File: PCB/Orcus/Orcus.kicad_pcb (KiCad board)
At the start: 2 copper layers, 258.2 x 87.7 mm, 84 parts, among them J1 -, J2 -, J3 +, J4 +, J5 LED, J6 LED, SW1 MX_LED, SW10 MX_LED, SW11 MX_LED, SW12 MX_LED, SW13 MX_LED, SW14 MX_LED, SW15 MX_LED, SW16 MX_LED, SW17 MX_LED, SW18 MX_LED, SW19 MX_LED, SW2 MX_LED, SW20 MX_LED, SW21 MX_LED, SW22 MX_LED, SW23 MX_LED, SW24 MX_LED, SW25 MX_LED, SW26 MX_LED, SW27 MX_LED, SW28 MX_LED, SW29 MX_LED, SW3 MX_LED, SW30 MX_LED, SW31 MX_LED, SW32 MX_LED, SW33 MX_LED, SW34 MX_LED, SW35 MX_LED, SW36 MX_LED, SW37 MX_LED, SW38 MX_LED, SW4 MX_LED, SW5 MX_LED, SW6 MX_LED, SW7 MX_LED, SW8 MX_LED, SW9 MX_LED, U1 XIAO-nRF52840-SMD, U3 XIAO-nRF52840-SMD

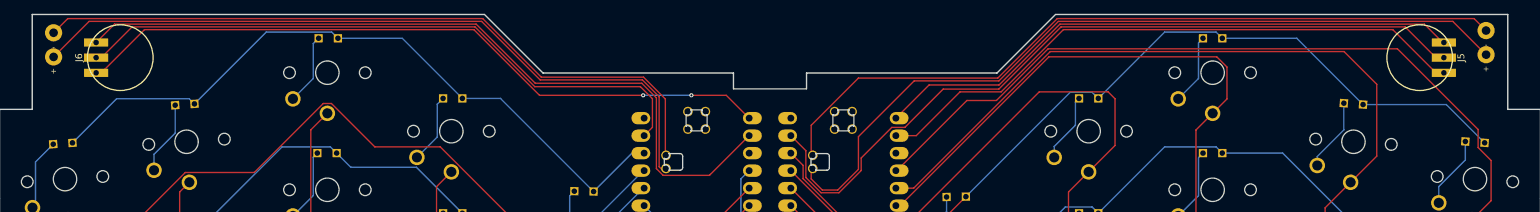
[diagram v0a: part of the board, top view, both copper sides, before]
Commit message: replaced pad
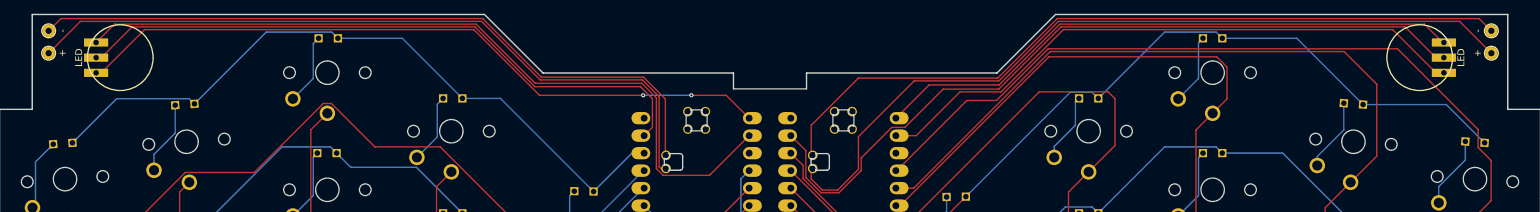
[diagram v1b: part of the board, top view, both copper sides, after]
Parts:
- +: renamed from J3; footprint TOTEMlib:BatteryPad -> Keebio-Parts.pretty-master:Wire_Pad_24AWG
- +: renamed from J4; footprint TOTEMlib:BatteryPad -> Keebio-Parts.pretty-master:Wire_Pad_24AWG
- -: renamed from J2; footprint TOTEMlib:BatteryPad -> Keebio-Parts.pretty-master:Wire_Pad_24AWG
- -: renamed from J1; footprint TOTEMlib:BatteryPad -> Keebio-Parts.pretty-master:Wire_Pad_24AWG
- moved + 0.90 mm to (42.9, 37.9), turned to -90 degrees
- moved + 0.80 mm to (252.4, 37.9), turned to 90 degrees
- moved - 0.78 mm to (42.9, 34.6), turned to -90 degrees
- moved - 0.77 mm to (252.4, 34.6), turned to 90 degrees
- renumbered J5 to LED, J6 to LED
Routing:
- net Net-(J1-Pin_1): track 109.3 -> 110.0 mm
- net Net-(J3-Pin_1): track 114.9 -> 115.6 mm
- net Net-(J2-Pin_1): track 102.1 -> 102.7 mm

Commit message: updated pcb and sch
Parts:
- removed LED (x2): LED, Keebio-Parts.pretty-master:NeoPixel_Mini_Button-v2
- added J5: LED, Keebio-Parts.pretty-master:NeoPixel_Mini_Button-v2, F.Cu at (242.0, 38.5)
- added J6: LED, Keebio-Parts.pretty-master:NeoPixel_Mini_Button-v2, F.Cu at (53.3, 38.5)
- D1, D10, D11, D12, D13, D14, D15, D16, D17, D18, D19, D2, D20, D21, D22, D23, D24, D25, D26, D27, D28, D29, D3, D30, D31, D32, D33, D34, D35, D36, D37, D38, D4, D5, D6, D7, D8, D9: footprint Keebio-Parts.pretty-master:D_SOD123F-Hole -> Keebio-Parts.pretty-master:D_SOD123F
- moved D30 6.89 mm to (133.3, 76.4), turned to -91 degrees
- moved D6 6.61 mm to (161.9, 76.2), turned to 91 degrees
- turned SW30 to 89 degrees
- turned SW6 to -89 degrees
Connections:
- U1 pad 1: unconnected-(U1-PA02_A0_D0-Pad1) -> row0-1
- U1 pad 10: col3-1 -> unconnected-(U1-PA5_A9_D9_MISO-Pad10)
- U1 pad 11: col4-1 -> Data-1
- U1 pad 2: Data-1 -> row1-1
- U1 pad 3: row0-1 -> row2-1
- U1 pad 4: row1-1 -> row3-1
- U1 pad 5: row2-1 -> col2-1
- U1 pad 6: row3-1 -> col1-1
- U1 pad 8: col1-1 -> col3-1
- U1 pad 9: col2-1 -> col4-1
- U3 pad 1: unconnected-(U3-PA02_A0_D0-Pad1) -> row0
- U3 pad 10: col3 -> unconnected-(U3-PA5_A9_D9_MISO-Pad10)
- U3 pad 11: col4 -> Data
- U3 pad 2: Data -> row1
- U3 pad 3: row0 -> row2
- U3 pad 4: row1 -> row3
- U3 pad 5: row2 -> col2
- U3 pad 6: row3 -> col1
- U3 pad 8: col1 -> col3
- U3 pad 9: col2 -> col4
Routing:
- net col1-1: track 194.9 -> 158.4 mm
- net col2-1: track 160.4 -> 130.6 mm, vias 0 -> 1
- net col0-1: track 152.4 -> 177.7 mm
- net col3: track 163.6 -> 144.1 mm
- net Data: track 113.4 -> 94.6 mm
- net Data-1: track 92.8 -> 110.6 mm
- net col4: track 166.0 -> 151.5 mm
- net col4-1: track 87.1 -> 96.8 mm
- net row2: track 134.5 -> 141.2 mm
- net col2: track 141.0 -> 147.3 mm
- net row0-1: track 102.2 -> 108.4 mm
- net row2-1: track 127.1 -> 132.7 mm
- net row3: track 144.5 -> 149.7 mm
- net row1-1: track 115.7 -> 120.7 mm
- net row1: track 126.2 -> 130.1 mm
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- added copper zone on B.Cu, net (none)
- added copper zone on F.Cu, net (none)

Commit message: update pcb
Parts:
- added Ref**: Mouse_Bite, Keebio-Parts.pretty-master:MouseBites_6x05mm_P1mm_Verical, F.Cu at (147.6, 67.5)
- moved U1 1.00 mm to (137.0, 53.9)
- moved U3 1.00 mm to (158.3, 53.9)
- renumbered J5 to LED, J6 to LED
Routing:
- net row1: track 130.1 -> 131.3 mm
- net Net-(J3-Pin_1): track 114.3 -> 115.4 mm
- net Net-(J4-Pin_1): track 105.3 -> 104.3 mm
- net row3: track 149.7 -> 150.7 mm
- net row2: track 141.2 -> 142.2 mm
- net row1-1: track 120.7 -> 121.7 mm
- net col4-1: track 96.8 -> 97.8 mm
- net col0: track 91.6 -> 92.6 mm
- net Net-(J2-Pin_1): track 102.3 -> 101.3 mm
- net row3-1: track 152.4 -> 153.4 mm
- net 5v-1: track 102.3 -> 103.2 mm
- net col0-1: track 177.7 -> 178.3 mm
- net row2-1: track 132.7 -> 133.3 mm
- net Data-1: track 110.6 -> 111.1 mm

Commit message: new sch
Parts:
- removed + (x2): +, Keebio-Parts.pretty-master:Wire_Pad_24AWG
- removed - (x2): -, Keebio-Parts.pretty-master:Wire_Pad_24AWG
- removed D1, D10, D11, D12, D13, D14, D15, D16, D17, D18, D19, D2, D20, D21, D22, D23, D24, D25, D26, D27, D28, D29, D3, D30, D31, D32, D33, D34, D35, D36, D37, D38, D4, D5, D6, D7, D8, D9: D, Keebio-Parts.pretty-master:D_SOD123F
- removed LED (x2): LED, Keebio-Parts.pretty-master:NeoPixel_Mini_Button-v2
- removed Ref**: Mouse_Bite, Keebio-Parts.pretty-master:MouseBites_6x05mm_P1mm_Verical
- removed SW1, SW10, SW11, SW12, SW13, SW14, SW15, SW16, SW17, SW18, SW19, SW2, SW20, SW21, SW22, SW23, SW24, SW25, SW26, SW27, SW28, SW29, SW3, SW30, SW31, SW32, SW33, SW34, SW35, SW36, SW37, SW38, SW4, SW5, SW6, SW7, SW8, SW9: MX_LED, Keebio-Parts.pretty-master:Kailh-PG1350-1u-NoLED
- removed U1, U3: XIAO-nRF52840-SMD, TOTEMlib:xiao-ble-smd-cutout-mod
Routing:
- net col0-1: track 178.3 -> 0.00 mm
- net col1-1: track 158.0 -> 0.00 mm
- net row3-1: track 153.4 -> 0.00 mm
- net col4: track 151.1 -> 0.00 mm
- net row3: track 150.7 -> 0.00 mm
- net col2: track 147.7 -> 0.00 mm
- net col3: track 143.7 -> 0.00 mm
- net row2: track 142.2 -> 0.00 mm
- net row2-1: track 133.3 -> 0.00 mm
- net row1: track 131.3 -> 0.00 mm
- net col2-1: track 130.1 -> 0.00 mm, vias 1 -> 0
- net row0: track 123.3 -> 0.00 mm
- net row1-1: track 121.7 -> 0.00 mm
- net Net-(J3-Pin_1): track 115.4 -> 0.00 mm
- net Gnd-1: track 112.6 -> 0.00 mm
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- removed copper zone on B.Cu, net (none)
- removed copper zone on F.Cu, net (none)
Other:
- board outline removed

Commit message: updated pcb
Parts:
- added D1: D, Keebio-Parts.pretty-master:D_SOD123F, B.Cu at (218.5, 105.0)
- added D10: D, Keebio-Parts.pretty-master:D_SOD123F, B.Cu at (211.5, 105.0)
- added D11: D, Keebio-Parts.pretty-master:D_SOD123F, B.Cu at (204.5, 94.5)
- added D12: D, Keebio-Parts.pretty-master:D_SOD123F, B.Cu at (204.5, 97.1)
- added D13: D, Keebio-Parts.pretty-master:D_SOD123F, B.Cu at (204.5, 99.7)
- added D14: D, Keebio-Parts.pretty-master:D_SOD123F, B.Cu at (204.5, 102.5)
- added D15: D, Keebio-Parts.pretty-master:D_SOD123F, B.Cu at (204.5, 105.1)
- added D16: D, Keebio-Parts.pretty-master:D_SOD123F, B.Cu at (197.5, 99.7)
- added D17: D, Keebio-Parts.pretty-master:D_SOD123F, B.Cu at (197.5, 94.5)
- added D18: D, Keebio-Parts.pretty-master:D_SOD123F, B.Cu at (197.5, 97.1)
- added D19: D, Keebio-Parts.pretty-master:D_SOD123F, B.Cu at (197.5, 102.5)
- added D2: D, Keebio-Parts.pretty-master:D_SOD123F, B.Cu at (218.5, 102.5)
- added D20: D, Keebio-Parts.pretty-master:D_SOD123F, F.Cu at (38.5, -7.50)
- added D21: D, Keebio-Parts.pretty-master:D_SOD123F, F.Cu at (37.3, -2.91)
- added D22: D, Keebio-Parts.pretty-master:D_SOD123F, F.Cu at (37.3, -0.31)
- added D23: D, Keebio-Parts.pretty-master:D_SOD123F, F.Cu at (37.3, 2.29)
- added D24: D, Keebio-Parts.pretty-master:D_SOD123F, F.Cu at (37.3, 4.89)
- added D25: D, Keebio-Parts.pretty-master:D_SOD123F, F.Cu at (37.3, 7.49)
- added D26: D, Keebio-Parts.pretty-master:D_SOD123F, F.Cu at (37.3, 10.1)
- added D27: D, Keebio-Parts.pretty-master:D_SOD123F, F.Cu at (37.3, 12.7)
- added D28: D, Keebio-Parts.pretty-master:D_SOD123F, F.Cu at (37.3, 15.3)
- added D29: D, Keebio-Parts.pretty-master:D_SOD123F, F.Cu at (37.3, 17.9)
- added D3: D, Keebio-Parts.pretty-master:D_SOD123F, B.Cu at (218.5, 99.7)
- added D30: D, Keebio-Parts.pretty-master:D_SOD123F, F.Cu at (37.3, 20.5)
- added D31: D, Keebio-Parts.pretty-master:D_SOD123F, F.Cu at (43.3, -2.91)
- added D32: D, Keebio-Parts.pretty-master:D_SOD123F, F.Cu at (43.3, -0.31)
- added D33: D, Keebio-Parts.pretty-master:D_SOD123F, F.Cu at (43.3, 2.29)
- added D34: D, Keebio-Parts.pretty-master:D_SOD123F, F.Cu at (43.3, 4.89)
- added D35: D, Keebio-Parts.pretty-master:D_SOD123F, F.Cu at (43.3, 7.49)
- added D36: D, Keebio-Parts.pretty-master:D_SOD123F, F.Cu at (43.3, 10.1)
- added D37: D, Keebio-Parts.pretty-master:D_SOD123F, F.Cu at (43.3, 12.7)
- added D38: D, Keebio-Parts.pretty-master:D_SOD123F, F.Cu at (43.3, 15.3)
- added D4: D, Keebio-Parts.pretty-master:D_SOD123F, B.Cu at (218.5, 97.0)
- added D5: D, Keebio-Parts.pretty-master:D_SOD123F, B.Cu at (218.5, 94.5)
- added D6: D, Keebio-Parts.pretty-master:D_SOD123F, B.Cu at (211.5, 94.5)
- added D7: D, Keebio-Parts.pretty-master:D_SOD123F, B.Cu at (211.5, 97.1)
- added D8: D, Keebio-Parts.pretty-master:D_SOD123F, B.Cu at (211.5, 99.7)
- added D9: D, Keebio-Parts.pretty-master:D_SOD123F, B.Cu at (211.5, 102.3)
- added SW1: MX_LED, Keebio-Parts.pretty-master:Kailh-PG1350-1u-NoLED, F.Cu at (178.7, 63.2)
- added SW10: MX_LED, Keebio-Parts.pretty-master:Kailh-PG1350-1u-NoLED, F.Cu at (252.8, 73.1)
- added SW11: MX_LED, Keebio-Parts.pretty-master:Kailh-PG1350-1u-NoLED, F.Cu at (179.3, 97.2)
- added SW12: MX_LED, Keebio-Parts.pretty-master:Kailh-PG1350-1u-NoLED, F.Cu at (197.9, 83.2)
- added SW13: MX_LED, Keebio-Parts.pretty-master:Kailh-PG1350-1u-NoLED, F.Cu at (215.9, 74.7)
- added SW14: MX_LED, Keebio-Parts.pretty-master:Kailh-PG1350-1u-NoLED, F.Cu at (233.9, 84.7)
- added SW15: MX_LED, Keebio-Parts.pretty-master:Kailh-PG1350-1u-NoLED, F.Cu at (251.5, 90.1)
- added SW16: MX_LED, Keebio-Parts.pretty-master:Kailh-PG1350-1u-NoLED, F.Cu at (161.3, 76.2)
- added SW17: MX_LED, Keebio-Parts.pretty-master:Kailh-PG1350-1u-NoLED, F.Cu at (232.3, 105.9)
- added SW18: MX_LED, Keebio-Parts.pretty-master:Kailh-PG1350-1u-NoLED, F.Cu at (250.2, 107.0)
- added SW19: MX_LED, Keebio-Parts.pretty-master:Kailh-PG1350-1u-NoLED, F.Cu at (269.7, 104.7)
- added SW2: MX_LED, Keebio-Parts.pretty-master:Kailh-PG1350-1u-NoLED, F.Cu at (197.9, 49.2)
- added SW20: MX_LED, Keebio-Parts.pretty-master:Kailh-PG1350-1u-NoLED, F.Cu at (117.6, 63.2)
- added SW21: MX_LED, Keebio-Parts.pretty-master:Kailh-PG1350-1u-NoLED, F.Cu at (98.4, 49.2)
- added SW22: MX_LED, Keebio-Parts.pretty-master:Kailh-PG1350-1u-NoLED, F.Cu at (80.4, 40.7)
- added SW23: MX_LED, Keebio-Parts.pretty-master:Kailh-PG1350-1u-NoLED, F.Cu at (60.0, 50.7)
- added SW24: MX_LED, Keebio-Parts.pretty-master:Kailh-PG1350-1u-NoLED, F.Cu at (42.3, 56.2)
- added SW25: MX_LED, Keebio-Parts.pretty-master:Kailh-PG1350-1u-NoLED, F.Cu at (117.3, 80.2)
- added SW26: MX_LED, Keebio-Parts.pretty-master:Kailh-PG1350-1u-NoLED, F.Cu at (98.4, 66.2)
- added SW27: MX_LED, Keebio-Parts.pretty-master:Kailh-PG1350-1u-NoLED, F.Cu at (80.4, 57.7)
- added SW28: MX_LED, Keebio-Parts.pretty-master:Kailh-PG1350-1u-NoLED, F.Cu at (61.2, 67.7)
- added SW29: MX_LED, Keebio-Parts.pretty-master:Kailh-PG1350-1u-NoLED, F.Cu at (43.6, 73.1)
- added SW3: MX_LED, Keebio-Parts.pretty-master:Kailh-PG1350-1u-NoLED, F.Cu at (215.9, 40.7)
- added SW30: MX_LED, Keebio-Parts.pretty-master:Kailh-PG1350-1u-NoLED, F.Cu at (117.0, 97.2)
- added SW31: MX_LED, Keebio-Parts.pretty-master:Kailh-PG1350-1u-NoLED, F.Cu at (98.4, 83.2)
- added SW32: MX_LED, Keebio-Parts.pretty-master:Kailh-PG1350-1u-NoLED, F.Cu at (80.4, 74.7)
- added SW33: MX_LED, Keebio-Parts.pretty-master:Kailh-PG1350-1u-NoLED, F.Cu at (62.5, 84.7)
- added SW34: MX_LED, Keebio-Parts.pretty-master:Kailh-PG1350-1u-NoLED, F.Cu at (44.8, 90.1)
- added SW35: MX_LED, Keebio-Parts.pretty-master:Kailh-PG1350-1u-NoLED, F.Cu at (135.0, 76.2)
- added SW36: MX_LED, Keebio-Parts.pretty-master:Kailh-PG1350-1u-NoLED, F.Cu at (64.0, 105.9)
- added SW37: MX_LED, Keebio-Parts.pretty-master:Kailh-PG1350-1u-NoLED, F.Cu at (46.1, 107.0)
- added SW38: MX_LED, Keebio-Parts.pretty-master:Kailh-PG1350-1u-NoLED, F.Cu at (26.6, 104.7)
- added SW39: MX_LED, Keebio-Parts.pretty-master:Kailh-PG1350-1u-NoLED, F.Cu at (-9.70, -5.05)
- added SW4: MX_LED, Keebio-Parts.pretty-master:Kailh-PG1350-1u-NoLED, F.Cu at (236.4, 50.7)
- added SW40: MX_LED, Keebio-Parts.pretty-master:Kailh-PG1350-1u-NoLED, F.Cu at (-9.70, 4.67)
- added SW5: MX_LED, Keebio-Parts.pretty-master:Kailh-PG1350-1u-NoLED, F.Cu at (254.0, 56.2)
- added SW6: MX_LED, Keebio-Parts.pretty-master:Kailh-PG1350-1u-NoLED, F.Cu at (179.0, 80.2)
- added SW7: MX_LED, Keebio-Parts.pretty-master:Kailh-PG1350-1u-NoLED, F.Cu at (197.9, 66.2)
- added SW8: MX_LED, Keebio-Parts.pretty-master:Kailh-PG1350-1u-NoLED, F.Cu at (215.9, 57.7)
- added SW9: MX_LED, Keebio-Parts.pretty-master:Kailh-PG1350-1u-NoLED, F.Cu at (235.1, 67.7)
- added U1: XIAO-nRF52840-DIP, SeeedStudio_XIAO_nRF52840_v1.1_KiCAD:XIAO-nRF52840-DIP, F.Cu at (161.0, 54.2)
- added U2: XIAO-nRF52840-DIP, SeeedStudio_XIAO_nRF52840_v1.1_KiCAD:XIAO-nRF52840-DIP, F.Cu at (135.3, 54.2)
- added mouse-bite-5mm-slot: VAL**, Keebio-Parts.pretty-master:mouse-bite-5mm-slot-jlc, F.Cu at (148.2, 50.8)
- added mouse-bite-5mm-slot: VAL**, Keebio-Parts.pretty-master:mouse-bite-5mm-slot-jlc, F.Cu at (148.2, 83.8)
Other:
- board outline added: 265.2 x 87.7 mm

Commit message: pcb update
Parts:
- added SW41: BATT, Keebio-Parts.pretty-master:Reset_Breakout, F.Cu at (178.0, 52.9)
- added SW42: BATT, Keebio-Parts.pretty-master:Reset_Breakout, F.Cu at (256.4, 37.5)
- added SW43: BATT, Keebio-Parts.pretty-master:Reset_Breakout, F.Cu at (39.9, 37.5)
- added SW44: BATT, Keebio-Parts.pretty-master:Reset_Breakout, F.Cu at (118.2, 52.9)
- D20, D21, D22, D23, D24, D25, D26, D27, D28, D29, D30, D31, D32, D33, D34, D35, D36, D37, D38: moved to B.Cu
- SW39, SW40: value MX_LED -> RESET; footprint Keebio-Parts.pretty-master:Kailh-PG1350-1u-NoLED -> Keebio-Parts.pretty-master:SW_SPST_TL3342
- moved SW39 192.1 mm to (175.6, 45.6), turned to 180 degrees
- moved SW40 136.7 mm to (120.7, 45.6), turned to 180 degrees
- moved D20 119.8 mm to (96.0, 97.6), turned to 180 degrees
- moved D31 116.4 mm to (96.0, 100.8), turned to 180 degrees
- moved D23 114.5 mm to (83.3, 107.2), turned to 180 degrees
- moved D21 113.4 mm to (89.7, 97.6), turned to 180 degrees
- moved D32 111.3 mm to (89.7, 100.8), turned to 180 degrees
- moved D22 108.2 mm to (83.3, 97.6), turned to 180 degrees
- moved D35 107.8 mm to (102.4, 97.6), turned to 180 degrees
- moved D33 106.3 mm to (83.3, 100.8), turned to 180 degrees
- moved D36 105.8 mm to (77.0, 110.3), turned to 180 degrees
- moved D25 105.0 mm to (96.0, 94.5), turned to 180 degrees
- moved D24 103.8 mm to (77.0, 100.8), turned to 180 degrees
- moved D37 100.3 mm to (77.0, 107.2), turned to 180 degrees
- moved D28 99.9 mm to (83.3, 104.0), turned to 180 degrees
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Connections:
- U1 pad 1: L-row0 -> unconnected-(U1-PA02_A0_D0-Pad1)
- U1 pad 10: unconnected-(U1-PA5_A9_D9_MISO-Pad10)_1 -> L-col3
- U1 pad 11: unconnected-(U1-PA6_A10_D10_MOSI-Pad11) -> L-col4
- U1 pad 2: L-row1 -> unconnected-(U1-PA4_A1_D1-Pad2)
- U1 pad 3: L-row2 -> L-row0
- U1 pad 4: L-row3 -> L-row1
- U1 pad 5: L-col2 -> L-row2
- U1 pad 6: L-col1 -> L-row3
- U1 pad 8: L-col3 -> L-col1
- U1 pad 9: L-col4 -> L-col2
- U2 pad 1: R-row0 -> unconnected-(U2-PA02_A0_D0-Pad1)_1
- U2 pad 10: unconnected-(U2-PA5_A9_D9_MISO-Pad10) -> R-col3
- U2 pad 11: unconnected-(U2-PA6_A10_D10_MOSI-Pad11)_1 -> R-col4
- U2 pad 2: R-row1 -> unconnected-(U2-PA4_A1_D1-Pad2)
- U2 pad 3: R-row2 -> R-row0
- U2 pad 4: R-row3 -> R-row1
- U2 pad 5: R-col2 -> R-row2
- U2 pad 6: R-col1 -> R-row3
- U2 pad 8: R-col3 -> R-col1
- U2 pad 9: R-col4 -> R-col2
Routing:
- net R-col4: track 0.00 -> 213.8 mm, vias 0 -> 1
- net R-col2: track 0.00 -> 210.5 mm, vias 0 -> 4
- net L-col4: track 0.00 -> 198.5 mm, vias 0 -> 4
- net L-col3: track 0.00 -> 193.4 mm, vias 0 -> 2
- net L-col2: track 0.00 -> 180.0 mm, vias 0 -> 2
- net R-col1: track 0.00 -> 165.9 mm, vias 0 -> 4
- net R-col3: track 0.00 -> 162.0 mm
- net L-row0: track 0.00 -> 127.4 mm, vias 0 -> 6
- net L-row1: track 0.00 -> 116.0 mm, vias 0 -> 4
- net L-row2: track 0.00 -> 114.1 mm, vias 0 -> 3
- net R-row0: track 0.00 -> 110.7 mm, vias 0 -> 5
- net L-row3: track 0.00 -> 107.5 mm, vias 0 -> 1
- net L-col0: track 0.00 -> 106.8 mm, vias 0 -> 2
- net R-col0: track 0.00 -> 106.5 mm, vias 0 -> 2
- net Net-(D4-A): track 0.00 -> 103.2 mm
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- added copper zone on B.Cu, net (none)
- added copper zone on F.Cu, net (none)
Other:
- outline, holes or cut-outs redrawn
